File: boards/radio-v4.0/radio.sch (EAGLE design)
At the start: 29 parts, among them J1 HFW8R-1ST, J2 TC2050-IDC-NL, U1 ISM43340, U2 MPM3620GQV-P

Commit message: Design Review Changes
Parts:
- R10, R7, R8, R9: value 600 -> 200
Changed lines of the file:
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@@
 <part name="SUPPLY19" library="RoboJackets-Supplies" deviceset="+3.3V" device=""/>
 <part name="SUPPLY20" library="supply2" library_urn="urn:adsk.eagle:library:372" deviceset="GND" device=""/>
-<part name="R8" library="resistor" library_urn="urn:adsk.eagle:library:348" deviceset="R-US_" device="R0603" package3d_urn="urn:adsk.eagle:package:23555/2" value="600"/>
-<part name="R7" library="resistor" library_urn="urn:adsk.eagle:library:348" deviceset="R-US_" device="R0603" package3d_urn="urn:adsk.eagle:package:23555/2" value="600"/>
-<part name="R9" library="resistor" library_urn="urn:adsk.eagle:library:348" deviceset="R-US_" device="R0603" package3d_urn="urn:adsk.eagle:package:23555/2" value="600"/>
-<part name="R10" library="resistor" library_urn="urn:adsk.eagle:library:348" deviceset="R-US_" device="R0603" package3d_urn="urn:adsk.eagle:package:23555/2" value="600"/>
+<part name="R8" library="resistor" library_urn="urn:adsk.eagle:library:348" deviceset="R-US_" device="R0603" package3d_urn="urn:adsk.eagle:package:23555/2" value="200"/>
+<part name="R7" library="resistor" library_urn="urn:adsk.eagle:library:348" deviceset="R-US_" device="R0603" package3d_urn="urn:adsk.eagle:package:23555/2" value="200"/>
+<part name="R9" library="resistor" library_urn="urn:adsk.eagle:library:348" deviceset="R-US_" device="R0603" package3d_urn="urn:adsk.eagle:package:23555/2" value="200"/>
+<part name="R10" library="resistor" library_urn="urn:adsk.eagle:library:348" deviceset="R-US_" device="R0603" package3d_urn="urn:adsk.eagle:package:23555/2" value="200"/>
 <part name="D5" library="RoboJackets-LEDs" deviceset="LED-SMD" device="" technology="-GREEN" value="GREEN"/>
 <part name="D6" library="RoboJackets-LEDs" deviceset="LED-SMD" device="" technology="-YELLOW" value="YELLOW"/>

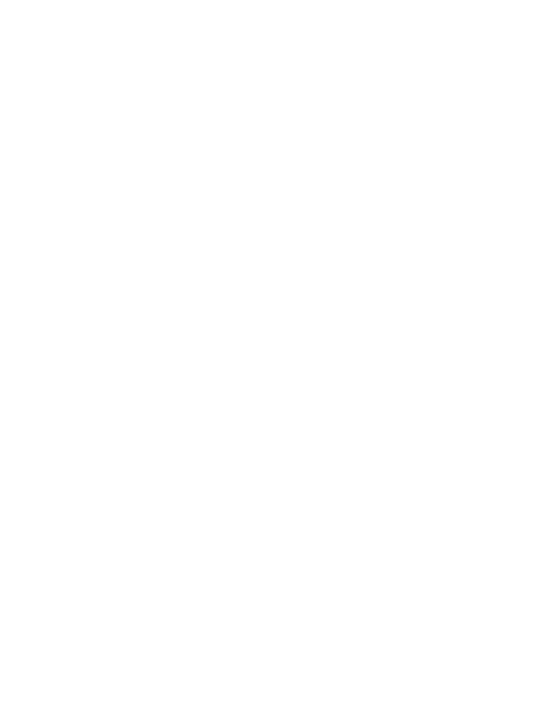
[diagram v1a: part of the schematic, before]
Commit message: J-Link Connector Added (NOT CONNECTED)
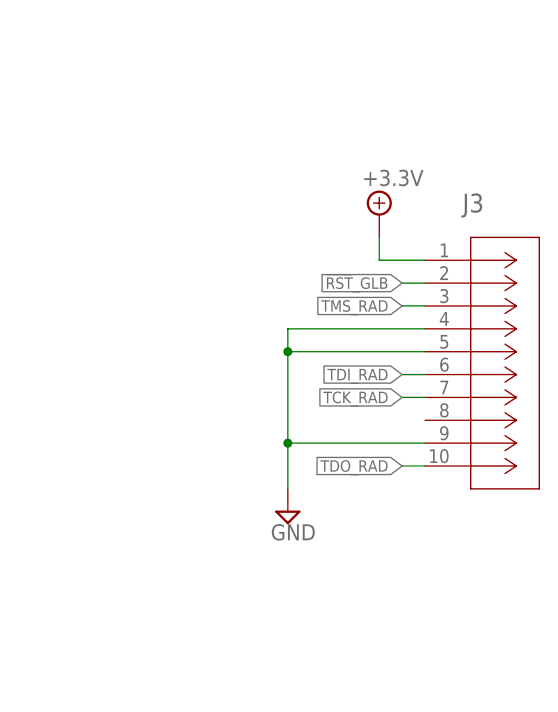
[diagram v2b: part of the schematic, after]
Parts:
- added J3: FTSH-105-01-F-D-K, Jlink-Connector:FTSH-105-01-F-D-K
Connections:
- net !RST!_GLB: now also J3.2
- net +3.3V: now also J3.1
- net GND: now also J3.4, J3.5, J3.9
- net TCK_RAD: now also J3.7
- net TDI_RAD: now also J3.6
- net TDO_RAD: now also J3.10
- net TMS_RAD: now also J3.3
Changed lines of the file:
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@@
 <part name="C3" library="rcl" library_urn="urn:adsk.eagle:library:334" deviceset="C-US" device="C0805" package3d_urn="urn:adsk.eagle:package:23617/2" value="10uF"/>
 <part name="C1" library="RoboJackets-Capacitors" deviceset="ECA-1HHG221" device="" override_package3d_urn="urn:adsk.eagle:package:33768299/2" override_package_urn="urn:adsk.eagle:footprint:33768301/1" value="220uF"/>
+<part name="J3" library="Jlink-Connector" deviceset="FTSH-105-01-F-D-K" device=""/>
+<part name="SUPPLY5" library="RoboJackets-Supplies" deviceset="+3.3V" device=""/>
+<part name="SUPPLY6" library="supply2" library_urn="urn:adsk.eagle:library:372" deviceset="GND" device=""/>
 </parts>
 <sheets>
@@
 <attribute name="NAME" x="42.1386" y="33.0708" size="1.778" layer="95" ratio="10" rot="SR0"/>
 </instance>
+<instance part="J3" gate="A" x="256.54" y="58.42" smashed="yes">
+<attribute name="NAME" x="260.7056" y="63.7286" size="2.0828" layer="95" ratio="6" rot="SR0"/>
+</instance>
+<instance part="SUPPLY5" gate="P" x="251.46" y="63.5" smashed="yes">
+<attribute name="VALUE" x="249.555" y="66.675" size="1.778" layer="96"/>
+</instance>
+<instance part="SUPPLY6" gate="GND" x="241.3" y="30.48" smashed="yes">
+<attribute name="VALUE" x="239.395" y="27.305" size="1.778" layer="96"/>
+</instance>
 </instances>
 <busses>
@@
 <pinref part="J2" gate="G$1" pin="1"/>
 <pinref part="SUPPLY19" gate="P" pin="+3.3V"/>
+</segment>
+<segment>
+<pinref part="J3" gate="A" pin="1"/>
+<wire x1="256.54" y1="58.42" x2="251.46" y2="58.42" width="0.1524" layer="91"/>
+<wire x1="251.46" y1="58.42" x2="251.46" y2="60.96" width="0.1524" layer="91"/>
+<pinref part="SUPPLY5" gate="P" pin="+3.3V"/>
 </segment>
 </net>
@@
 <pinref part="SUPPLY10" gate="GND" pin="GND"/>
 </segment>
+<segment>
+<pinref part="J3" gate="A" pin="5"/>
+<wire x1="256.54" y1="48.26" x2="241.3" y2="48.26" width="0.1524" layer="91"/>
+<wire x1="241.3" y1="48.26" x2="241.3" y2="38.1" width="0.1524" layer="91"/>
+<pinref part="J3" gate="A" pin="4"/>
+<wire x1="241.3" y1="38.1" x2="241.3" y2="33.02" width="0.1524" layer="91"/>
+<wire x1="256.54" y1="50.8" x2="241.3" y2="50.8" width="0.1524" layer="91"/>
+<wire x1="241.3" y1="50.8" x2="241.3" y2="48.26" width="0.1524" layer="91"/>
+<junction x="241.3" y="48.26"/>
+<pinref part="J3" gate="A" pin="9"/>
+<wire x1="256.54" y1="38.1" x2="241.3" y2="38.1" width="0.1524" layer="91"/>
+<junction x="241.3" y="38.1"/>
+<pinref part="SUPPLY6" gate="GND" pin="GND"/>
+</segment>
 </net>
 <net name="TMS_RAD" class="0">
@@
 <label x="170.18" y="33.02" size="1.27" layer="95" xref="yes"/>
 </segment>
+<segment>
+<pinref part="J3" gate="A" pin="3"/>
+<wire x1="256.54" y1="53.34" x2="254" y2="53.34" width="0.1524" layer="91"/>
+<label x="254" y="53.34" size="1.27" layer="95" rot="R180" xref="yes"/>
+</segment>
 </net>
 <net name="TCK_RAD" class="0">
@@
 <label x="170.18" y="30.48" size="1.27" layer="95" xref="yes"/>
 </segment>
+<segment>
+<pinref part="J3" gate="A" pin="7"/>
+<wire x1="256.54" y1="43.18" x2="254" y2="43.18" width="0.1524" layer="91"/>
+<label x="254" y="43.18" size="1.27" layer="95" rot="R180" xref="yes"/>
+</segment>
 </net>
 <net name="TDI_RAD" class="0">
@@
 <label x="170.18" y="25.4" size="1.27" layer="95" xref="yes"/>
 </segment>
+<segment>
+<pinref part="J3" gate="A" pin="6"/>
+<wire x1="256.54" y1="45.72" x2="254" y2="45.72" width="0.1524" layer="91"/>
+<label x="254" y="45.72" size="1.27" layer="95" rot="R180" xref="yes"/>
+</segment>
 </net>
 <net name="TDO_RAD" class="0">
@@
 <wire x1="167.64" y1="27.94" x2="170.18" y2="27.94" width="0.1524" layer="91"/>
 <label x="170.18" y="27.94" size="1.27" layer="95" xref="yes"/>
+</segment>
+<segment>
+<pinref part="J3" gate="A" pin="10"/>
+<wire x1="256.54" y1="35.56" x2="254" y2="35.56" width="0.1524" layer="91"/>
+<label x="254" y="35.56" size="1.27" layer="95" rot="R180" xref="yes"/>
 </segment>
 </net>
@@
 <label x="170.18" y="22.86" size="1.27" layer="95" xref="yes"/>
 </segment>
-</net>
+<segment>
+<pinref part="J3" gate="A" pin="2"/>
+<wire x1="256.54" y1="55.88" x2="254" y2="55.88" width="0.1524" layer="91"/>
+<label x="254" y="55.88" size="1.27" layer="95" rot="R180" xref="yes"/>
+</segment>
+</net>

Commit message: JLINK Connector (CONNECTED)
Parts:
- removed J2: TC2050-IDC-NL, RoboJackets-Connectors:TC2050-IDC-NL
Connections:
- net !RST!_GLB: no longer J2.10
- net +3.3V: no longer J2.1
- net GND: no longer J2.3, J2.5, J2.9
- net TCK_RAD: no longer J2.4
- net TDI_RAD: no longer J2.8
- net TDO_RAD: no longer J2.6
- net TMS_RAD: no longer J2.2
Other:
- note removed: "GDET"
- note removed: "VREF"
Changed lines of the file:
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@@
 <part name="D3" library="RoboJackets-LEDs" deviceset="LED-SMD" device="" technology="-RED" value="RED"/>
 <part name="SUPPLY25" library="supply2" library_urn="urn:adsk.eagle:library:372" deviceset="GND" device=""/>
-<part name="J2" library="RoboJackets-Connectors" deviceset="TC2050-IDC-NL" device=""/>
-<part name="SUPPLY19" library="RoboJackets-Supplies" deviceset="+3.3V" device=""/>
-<part name="SUPPLY20" library="supply2" library_urn="urn:adsk.eagle:library:372" deviceset="GND" device=""/>
 <part name="R8" library="resistor" library_urn="urn:adsk.eagle:library:348" deviceset="R-US_" device="R0603" package3d_urn="urn:adsk.eagle:package:23555/2" value="200"/>
 <part name="R7" library="resistor" library_urn="urn:adsk.eagle:library:348" deviceset="R-US_" device="R0603" package3d_urn="urn:adsk.eagle:package:23555/2" value="200"/>
@@
 <wire x1="134.62" y1="7.62" x2="190.5" y2="7.62" width="0.1524" layer="97" style="shortdash"/>
 <wire x1="134.62" y1="55.88" x2="190.5" y2="55.88" width="0.1524" layer="97" style="shortdash"/>
-<text x="145.288" y="33.528" size="1.27" layer="97">VREF</text>
-<text x="145.288" y="23.368" size="1.27" layer="97">GDET</text>
 <text x="137.16" y="48.26" size="2.54" layer="97">JTAG - Radio FW Updates</text>
 <wire x1="190.5" y1="7.62" x2="190.5" y2="55.88" width="0.1524" layer="97" style="shortdash"/>
@@
 <attribute name="VALUE" x="236.855" y="197.485" size="1.778" layer="96"/>
 </instance>
-<instance part="J2" gate="G$1" x="157.48" y="27.94" smashed="yes">
-<attribute name="VALUE" x="152.654" y="36.576" size="1.27" layer="96"/>
-<attribute name="NAME" x="152.654" y="18.288" size="1.27" layer="95"/>
-</instance>
-<instance part="SUPPLY19" gate="P" x="144.78" y="38.1" smashed="yes">
-<attribute name="VALUE" x="142.875" y="41.275" size="1.778" layer="96"/>
-</instance>
-<instance part="SUPPLY20" gate="GND" x="144.78" y="15.24" smashed="yes">
-<attribute name="VALUE" x="142.875" y="12.065" size="1.778" layer="96"/>
-</instance>
 <instance part="R8" gate="G$1" x="220.98" y="241.3" smashed="yes">
 <attribute name="NAME" x="217.17" y="242.7986" size="1.778" layer="95"/>
@@
 <pinref part="C3" gate="G$1" pin="1"/>
 <pinref part="C1" gate="A" pin="11"/>
-</segment>
-<segment>
-<wire x1="147.32" y1="33.02" x2="144.78" y2="33.02" width="0.1524" layer="91"/>
-<wire x1="144.78" y1="33.02" x2="144.78" y2="35.56" width="0.1524" layer="91"/>
-<pinref part="J2" gate="G$1" pin="1"/>
-<pinref part="SUPPLY19" gate="P" pin="+3.3V"/>
 </segment>
 <segment>
@@
 </segment>
 <segment>
-<wire x1="147.32" y1="30.48" x2="144.78" y2="30.48" width="0.1524" layer="91"/>
-<wire x1="144.78" y1="30.48" x2="144.78" y2="27.94" width="0.1524" layer="91"/>
-<wire x1="144.78" y1="27.94" x2="144.78" y2="22.86" width="0.1524" layer="91"/>
-<wire x1="144.78" y1="22.86" x2="144.78" y2="17.78" width="0.1524" layer="91"/>
-<wire x1="147.32" y1="22.86" x2="144.78" y2="22.86" width="0.1524" layer="91"/>
-<junction x="144.78" y="22.86"/>
-<pinref part="J2" gate="G$1" pin="3"/>
-<pinref part="J2" gate="G$1" pin="9"/>
-<pinref part="SUPPLY20" gate="GND" pin="GND"/>
-<pinref part="J2" gate="G$1" pin="5"/>
-<wire x1="147.32" y1="27.94" x2="144.78" y2="27.94" width="0.1524" layer="91"/>
-<junction x="144.78" y="27.94"/>
-</segment>
-<segment>
 <pinref part="J1" gate="G$1" pin="2"/>
 <wire x1="213.36" y1="160.02" x2="215.9" y2="160.02" width="0.1524" layer="91"/>
@@
 </segment>
 <segment>
-<pinref part="J2" gate="G$1" pin="2"/>
-<wire x1="167.64" y1="33.02" x2="170.18" y2="33.02" width="0.1524" layer="91"/>
-<label x="170.18" y="33.02" size="1.27" layer="95" xref="yes"/>
-</segment>
-<segment>
 <pinref part="J3" gate="A" pin="3"/>
 <wire x1="256.54" y1="53.34" x2="254" y2="53.34" width="0.1524" layer="91"/>
@@
 </segment>
 <segment>
-<pinref part="J2" gate="G$1" pin="4"/>
-<wire x1="167.64" y1="30.48" x2="170.18" y2="30.48" width="0.1524" layer="91"/>
-<label x="170.18" y="30.48" size="1.27" layer="95" xref="yes"/>
-</segment>
-<segment>
 <pinref part="J3" gate="A" pin="7"/>
 <wire x1="256.54" y1="43.18" x2="254" y2="43.18" width="0.1524" layer="91"/>
@@
 </segment>
 <segment>
-<pinref part="J2" gate="G$1" pin="8"/>
-<wire x1="167.64" y1="25.4" x2="170.18" y2="25.4" width="0.1524" layer="91"/>
-<label x="170.18" y="25.4" size="1.27" layer="95" xref="yes"/>
-</segment>
-<segment>
 <pinref part="J3" gate="A" pin="6"/>
 <wire x1="256.54" y1="45.72" x2="254" y2="45.72" width="0.1524" layer="91"/>
@@
 <label x="60.96" y="162.56" size="1.27" layer="95" rot="R90" xref="yes"/>
 <pinref part="U1" gate="G$1" pin="P07-JTAG_TDO"/>
-</segment>
-<segment>
-<pinref part="J2" gate="G$1" pin="6"/>
-<wire x1="167.64" y1="27.94" x2="170.18" y2="27.94" width="0.1524" layer="91"/>
-<label x="170.18" y="27.94" size="1.27" layer="95" xref="yes"/>
 </segment>
 <segment>
@@
 </segment>
 <segment>
-<pinref part="J2" gate="G$1" pin="10"/>
-<wire x1="167.64" y1="22.86" x2="170.18" y2="22.86" width="0.1524" layer="91"/>
-<label x="170.18" y="22.86" size="1.27" layer="95" xref="yes"/>
-</segment>
-<segment>
